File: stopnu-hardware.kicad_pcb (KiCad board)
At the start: 4 copper layers, 150 x 128 mm, 47 parts, among them CN1 SM04B-SRSS-TB (LF)(SN), Q1 TEPT4400, U1 WIFI_KIT_32__V3_, U2 LTV-817M, U26 74LVC1G17GW,125, U3 LTV-817M, U4 LTV-817M

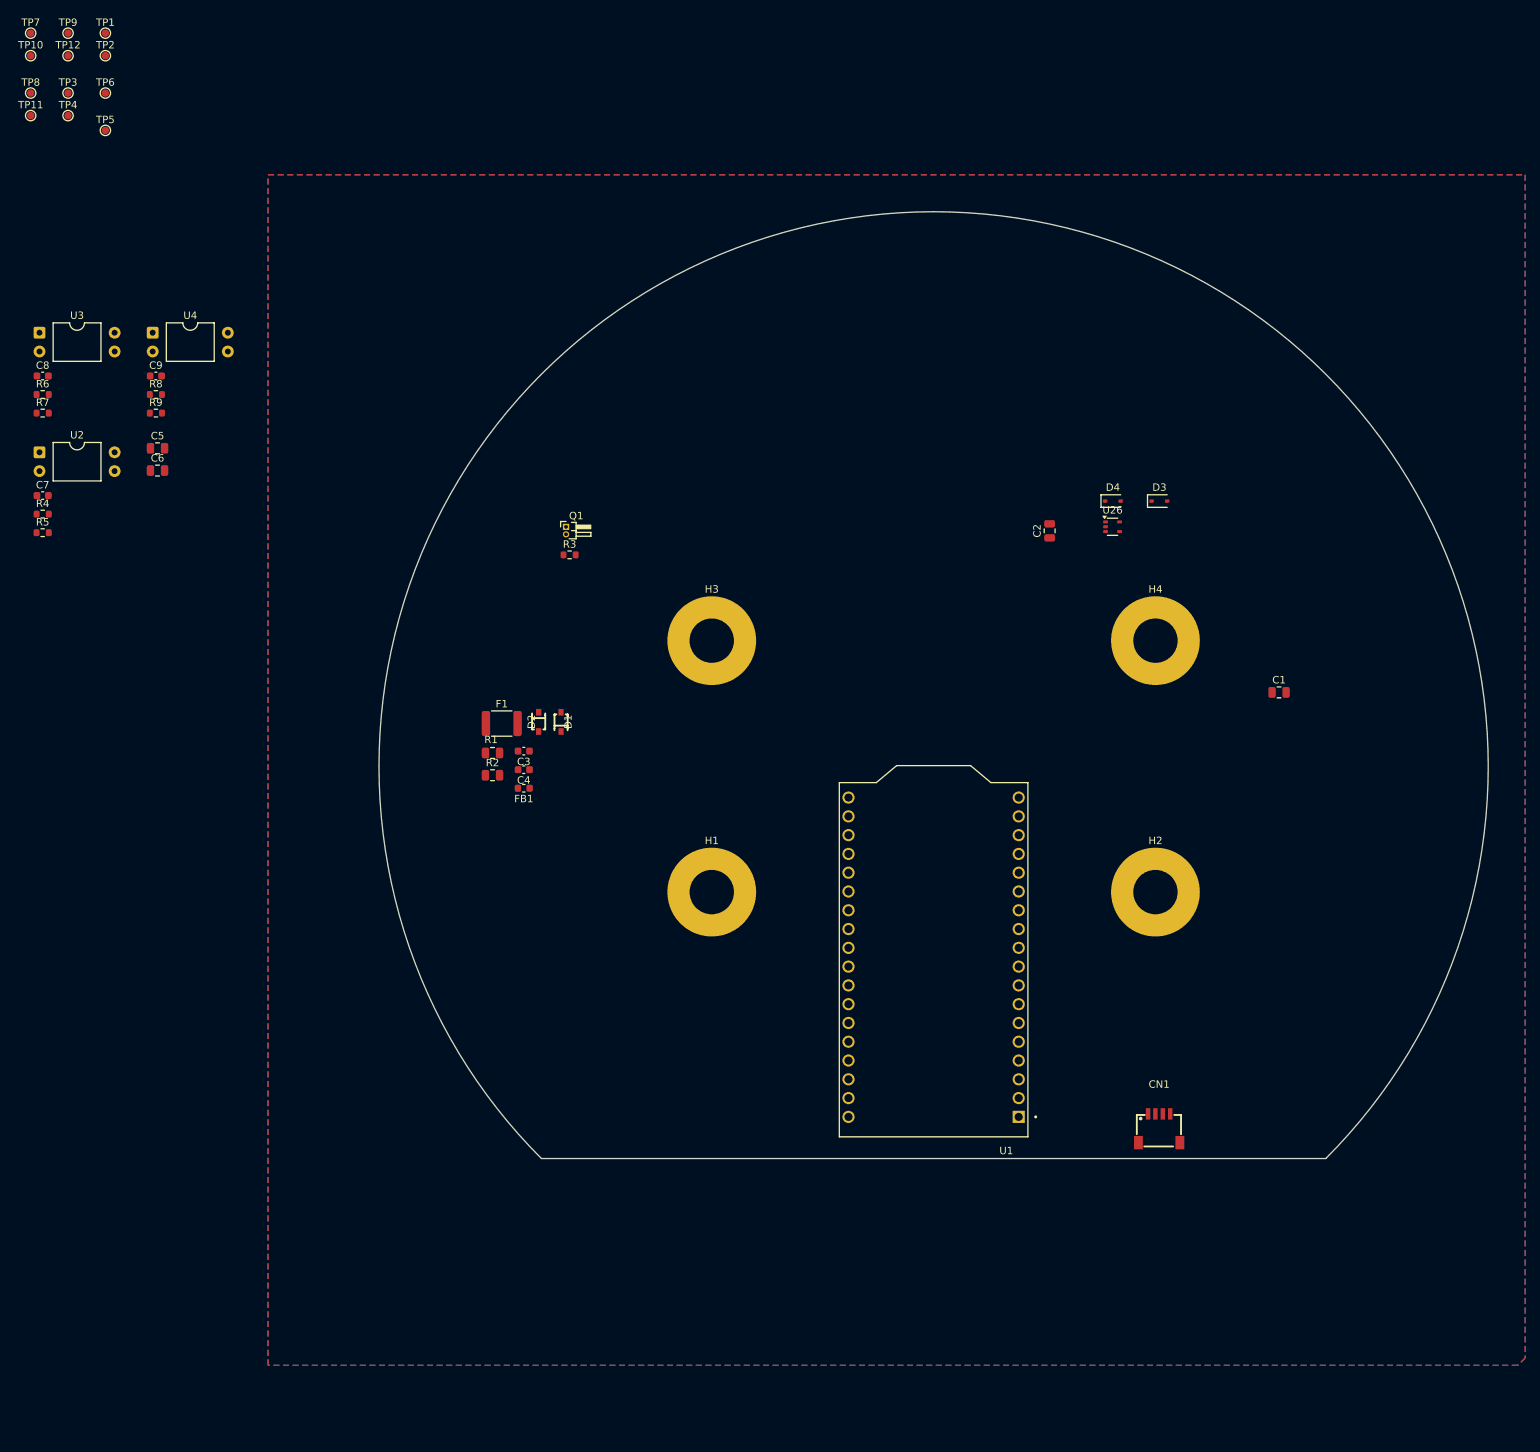
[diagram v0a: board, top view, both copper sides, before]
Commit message: Place opto couplers and some connectors.
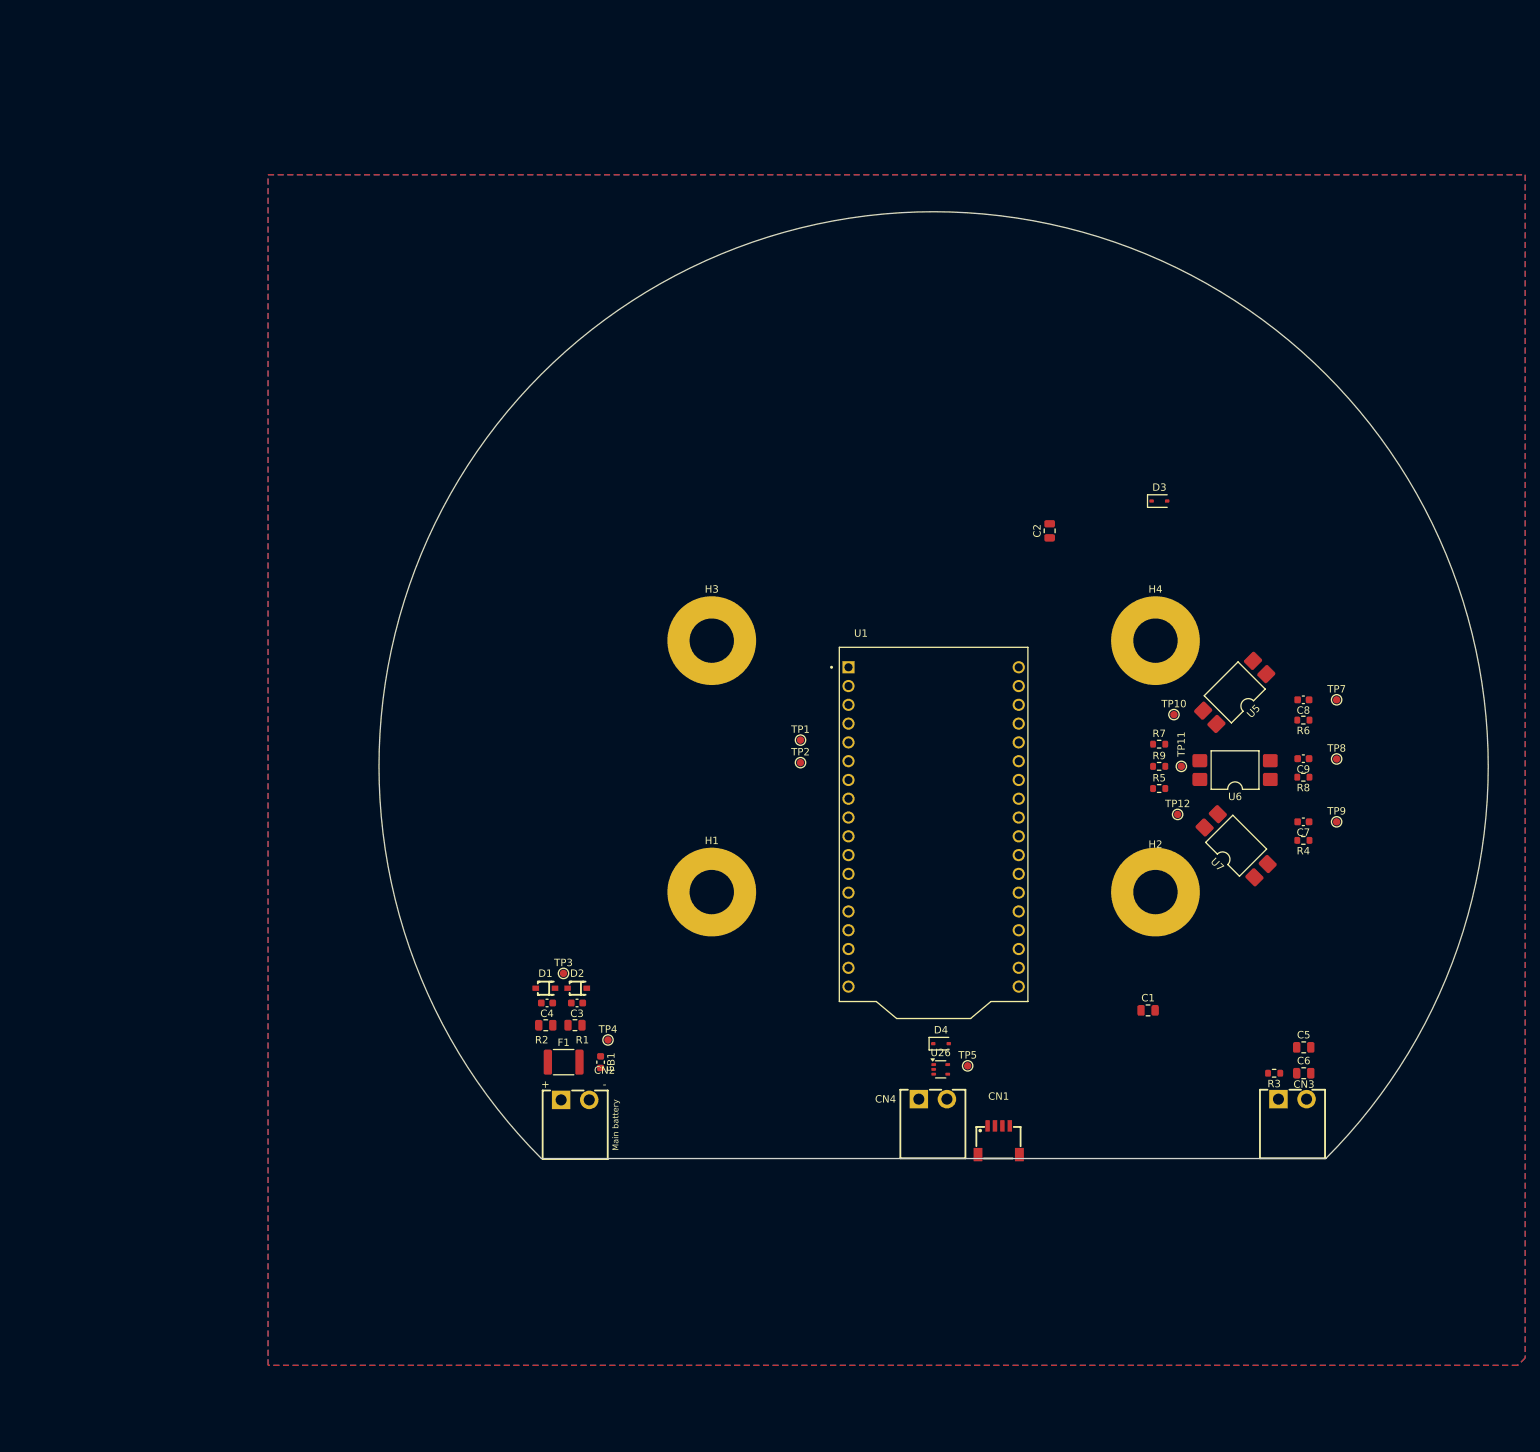
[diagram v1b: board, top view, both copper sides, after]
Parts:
- removed Q1: TEPT4400, Connector_PinHeader_1.00mm:PinHeader_1x02_P1.00mm_Horizontal
- removed TP6: TestPoint, TestPoint:TestPoint_Pad_D1.0mm
- removed U2, U3, U4: LTV-817M, Package_DIP:DIP-4_W10.16mm
- added CN2: OQ0232510000G, lcsc:CONN-TH_OQ0232510000G, F.Cu at (-48.5, 45.1)
- added CN3: OQ0232510000G, lcsc:CONN-TH_OQ0232510000G, F.Cu at (48.5, 45.0)
- added CN4: OQ0232510000G, lcsc:CONN-TH_OQ0232510000G, F.Cu at (-0.10, 45.0)
- added U5: LTV-817S, Package_DIP:SMDIP-4_W9.53mm, F.Cu at (40.7, -10.0)
- added U6: LTV-817S, Package_DIP:SMDIP-4_W9.53mm, F.Cu at (40.8, 0.50)
- added U7: LTV-817S, Package_DIP:SMDIP-4_W9.53mm, F.Cu at (40.9, 10.7)
- moved TP9 202.0 mm to (54.5, 7.50)
- moved TP7 198.3 mm to (54.5, -9.00)
- moved TP8 198.2 mm to (54.5, -1.00)
- moved TP12 181.8 mm to (33.0, 6.50)
- moved TP11 178.8 mm to (33.5, 0.00), turned to 90 degrees
- moved TP10 178.4 mm to (32.5, -7.00)
- moved C7 176.1 mm to (50.0, 7.50), turned to 180 degrees
- moved R4 176.1 mm to (50.0, 10.0), turned to 180 degrees
- moved R6 176.1 mm to (50.0, -6.25), turned to 180 degrees
- moved C8 176.0 mm to (50.0, -9.00), turned to 180 degrees
- moved C6 175.1 mm to (50.0, 41.5)
- moved C5 174.9 mm to (50.0, 38.0)
- moved TP5 172.0 mm to (4.61, 40.5)
- moved C9 163.6 mm to (50.0, -1.04), turned to 180 degrees
- moved R8 163.6 mm to (50.0, 1.47), turned to 180 degrees
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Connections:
- net /Ambient light sensor/V_AMLIGHT renamed /Ambient light sensor/V_AMLIGHT_EM
- net /battery_50v_to_adc/VBATT_OUT_3V3 renamed /battery_50v_to_adc/VBATT_LVL_OUT_LOW
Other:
- board text added: "USB-C cable Clearance"

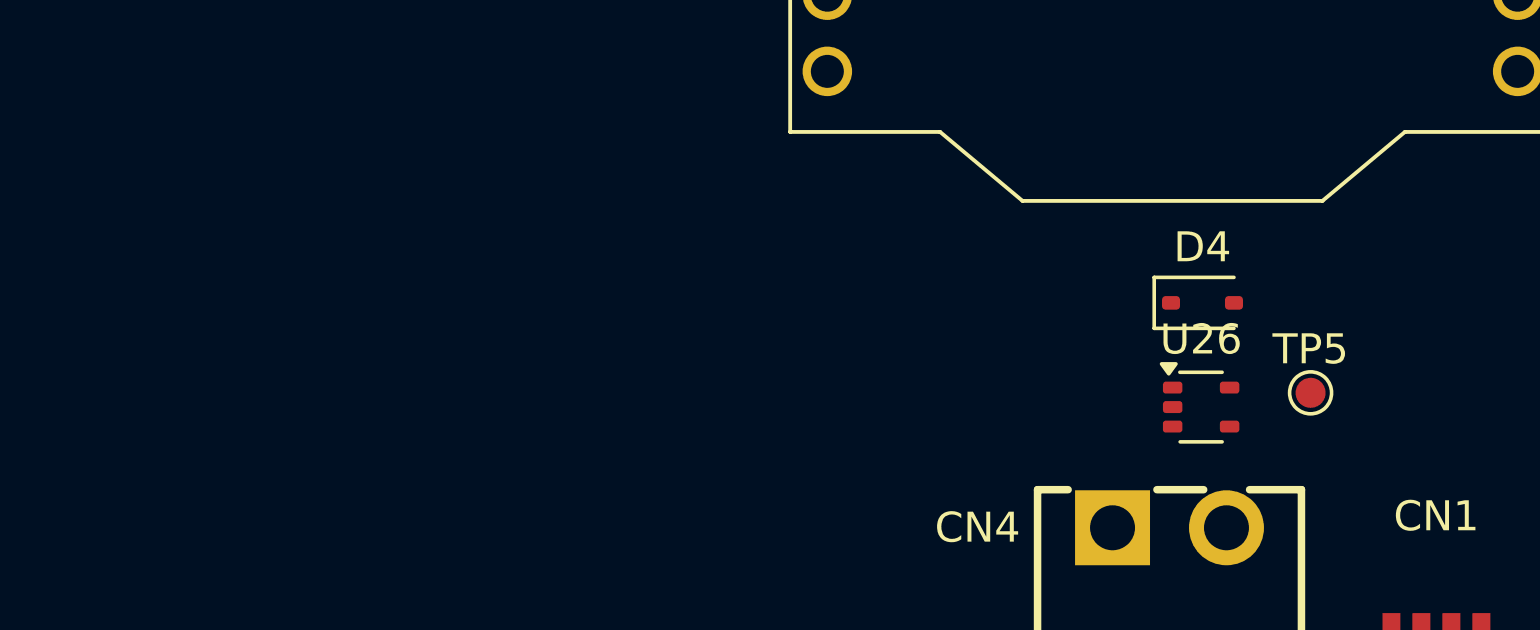
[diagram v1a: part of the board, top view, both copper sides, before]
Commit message: changed driver IC for LED signal to 74HCT1G125GW
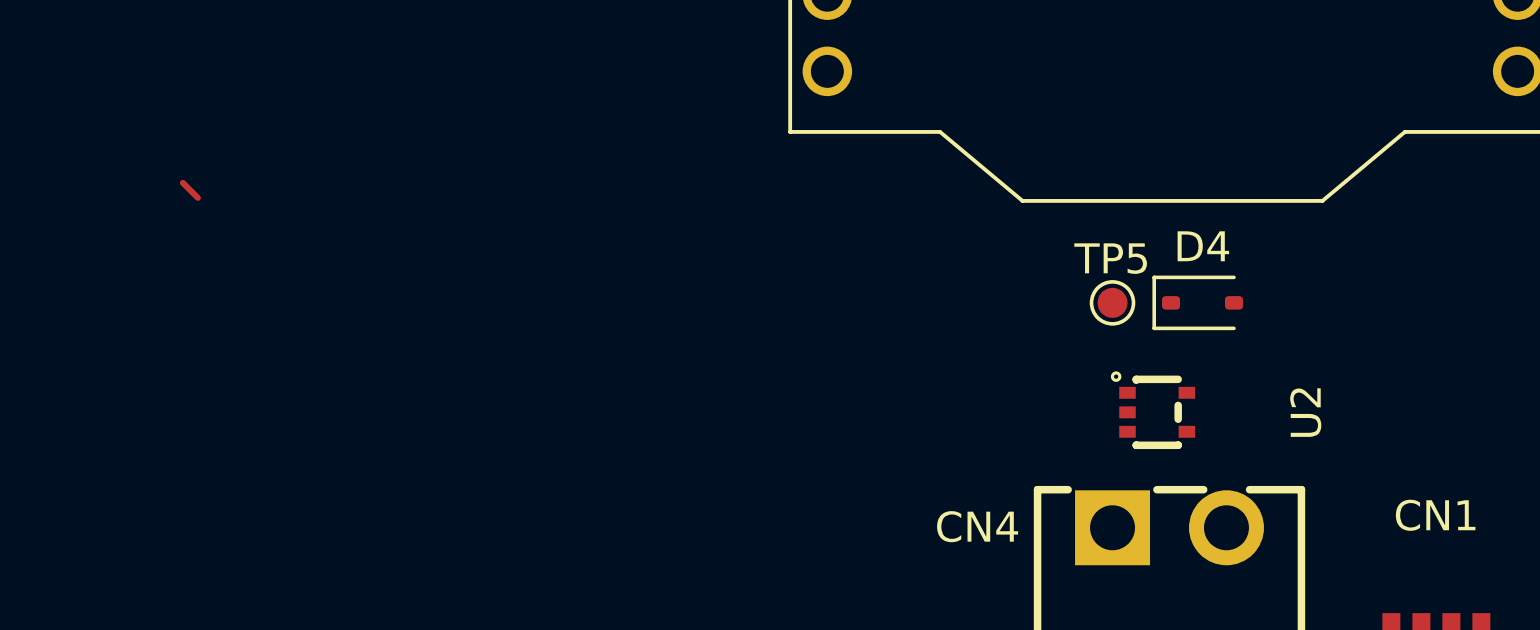
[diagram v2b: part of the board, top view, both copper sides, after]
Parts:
- removed U26: 74LVC1G17GW,125, Package_TO_SOT_SMD:SOT-353_SC-70-5
- added U2: 74HCT1G125GW-Q100H, lcsc:TSSOP-5_L2.1-W1.3-P0.65-LS2.2-BL, F.Cu at (-0.51, 41.1)
- moved TP5 7.25 mm to (-2.00, 37.5)
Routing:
- net (no net): track 0.00 -> 0.71 mm

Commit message: Push schematic stuff missed before.
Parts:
- added C10: 100nF, Capacitor_SMD:C_0805_2012Metric, F.Cu at (19.2, 29.0)
- added C11: C_Small, Capacitor_SMD:C_0603_1608Metric, F.Cu at (25.5, 31.3)
- added C12: C_Small, Capacitor_SMD:C_0603_1608Metric, F.Cu at (64.5, -3.00)
- added C13: C_Small, Capacitor_SMD:C_0603_1608Metric, F.Cu at (64.5, 35.0)
- added C14: C_Small, Capacitor_SMD:C_0603_1608Metric, F.Cu at (8.50, 38.7)
- added C15: 10u, Capacitor_SMD:C_0805_2012Metric, F.Cu at (54.1, -1.09)
- added C16: 100nF, Capacitor_SMD:C_0805_2012Metric, F.Cu at (54.1, 1.92)
- added C62: 10u, Capacitor_SMD:C_0805_2012Metric, F.Cu at (-37.2, 28.8)
- added C63: 10u, Capacitor_SMD:C_0805_2012Metric, F.Cu at (-33.3, 28.8)
- added CN5: OQ0232510000G, lcsc:CONN-TH_OQ0232510000G, F.Cu at (-34.5, 44.6)
- added CN6: OQ0432510000G, lcsc:CONN-TH_4P-P3.81_OQ0432510000G, F.Cu at (57.3, 44.5)
- added FB2: BLM18PG121SN1D, Inductor_SMD:L_0603_1608Metric, F.Cu at (-32.7, 40.1)
- added FB3: BLM18PG121SN1D, Inductor_SMD:L_0603_1608Metric, F.Cu at (-36.2, 40.1)
- added JP1: Jumper_2_Bridged, Jumper:SolderJumper-2_P1.3mm_Bridged_RoundedPad1.0x1.5mm, F.Cu at (17.5, -16.5)
- added JP2: Jumper_2_Open, Jumper:SolderJumper-2_P1.3mm_Open_RoundedPad1.0x1.5mm, F.Cu at (17.4, -20.5)
- added R53: 10k, Resistor_SMD:R_0402_1005Metric, F.Cu at (-30.2, 35.3)
- added R54: 6.8k, Resistor_SMD:R_0402_1005Metric, F.Cu at (-38.2, 35.3)
- added U19: SY6280AAC, Package_TO_SOT_SMD:SOT-23-5, F.Cu at (-34.1, 33.3)
- added U3: LD1117V33, lcsc:TO-220-3_L10.0-W4.5-P2.54-L, F.Cu at (53.5, -6.00)
- FB1: value FerriteBead_Small -> BLM18PG121SN1D
- moved TP10 49.2 mm to (55.5, 36.5)
- moved R7 44.4 mm to (55.5, 33.7), turned to -90 degrees
- moved TP11 44.2 mm to (58.5, 36.5), turned to 180 degrees
- moved R9 43.8 mm to (58.5, 33.7), turned to -90 degrees
- moved R5 37.7 mm to (52.5, 33.7), turned to -90 degrees
- moved C2 37.6 mm to (48.8, -13.9)
- moved U5 35.9 mm to (56.0, 22.5), turned to -90 degrees
- moved TP12 35.8 mm to (52.5, 36.5), turned to 135 degrees
- moved U6 31.4 mm to (63.2, 22.5), turned to -90 degrees
- moved D3 28.8 mm to (18.0, -10.0)
- moved C8 22.6 mm to (54.3, 13.2), turned to -90 degrees
- moved CN1 22.0 mm to (30.8, 49.6)
- moved R6 20.7 mm to (57.1, 13.2), turned to -90 degrees
- moved D4 19.9 mm to (20.9, 37.5)
- moved TP5 19.9 mm to (17.9, 37.5)
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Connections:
- D3 pad 1: +3.3V -> +3V3
- U1 pad J3_2: +3V3 -> /MCU/+3V3MCU
- U1 pad J3_3: +3V3 -> /MCU/+3V3MCU
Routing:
- net /battery_50v_to_adc/VBATT_LVL_OUT_LOW: track 0.00 -> 14.0 mm
- net /battery_50v_to_adc/VBATT_3_V50: track 0.00 -> 6.67 mm
- net /battery_50v_to_adc/VBATT_V50: track 0.00 -> 5.44 mm
- net /battery_50v_to_adc/VBATT_2_V50: track 0.00 -> 3.19 mm
- net VBATT: track 0.00 -> 2.54 mm
- net (no net): track 0.71 -> 0.00 mm
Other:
- board size 150 x 128 mm -> 140 x 106 mm
- board text added: "Bracket housing stay out"

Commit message: Some extra work for building the rats nest.
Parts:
- removed C10: 100nF, Capacitor_SMD:C_0805_2012Metric
- removed C3, C4: 10nF, Capacitor_SMD:C_0603_1608Metric
- removed CN2: OQ0232510000G, lcsc:CONN-TH_OQ0232510000G
- removed D1, D2: 1N4148WSG_C2904852, lcsc:SOD-323_L1.6-W1.3-LS2.7-RD
- removed F1: Polyfuse, Fuse:Fuse_1812_4532Metric
- removed FB1: BLM18PG121SN1D, Inductor_SMD:L_0603_1608Metric
- removed R1: 100k, Capacitor_SMD:C_0805_2012Metric
- removed R2: 3.6K, Capacitor_SMD:C_0805_2012Metric
- removed TP3, TP4: TestPoint, TestPoint:TestPoint_Pad_D1.0mm
- added J1: Conn_02x15_Odd_Even, Connector_PinHeader_2.54mm:PinHeader_2x15_P2.54mm_Horizontal, F.Cu at (-18.8, 14.0)
- H1, H2, H3, H4: footprint MountingHole:MountingHole_6mm_Pad -> MountingHole:MountingHole_6.4mm_M6_DIN965_Pad
- moved U3 81.6 mm to (-27.2, 6.19)
- moved C15 81.0 mm to (-26.0, 10.8), turned to -90 degrees
- moved C16 78.2 mm to (-23.0, 14.7), turned to -90 degrees
- moved D3 76.1 mm to (-20.3, 55.8), turned to 90 degrees
- moved C2 74.7 mm to (5.36, 46.9)
- moved TP8 72.3 mm to (11.8, 62.1), turned to -90 degrees
- moved R8 70.5 mm to (8.89, 57.7), turned to 90 degrees
- moved C9 65.9 mm to (11.9, 57.7), turned to 90 degrees
- moved JP1 64.3 mm to (-41.6, 8.86)
- moved JP2 64.3 mm to (-41.8, 4.86)
- moved C13 63.7 mm to (5.00, 57.7)
- moved TP7 63.6 mm to (19.2, 61.6), turned to -90 degrees
- moved TP1 62.5 mm to (-45.5, 52.6), turned to -90 degrees
- moved TP2 62.0 mm to (-45.5, 55.1), turned to -90 degrees
- moved R6 59.9 mm to (16.4, 57.2), turned to 90 degrees
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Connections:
- net /MCU/GPIO33 renamed /GPIO42
- net /MCU/MCU_VBAT_3V3 renamed /HELTEC V3/MCU_VBAT_3V3
- net Net-(U1A-U0RXD/GPIO44/CP2102_TX) renamed /UART_TX
- net Net-(U1A-U0TXD/GPIO43/CP2102_RX) renamed /UART_RX
- CN1 pad 3: /QWIIC_SDA -> /GPIO47
- CN1 pad 4: /QWIIC_SCL -> /GPIO48
- CN6 pad 2: /Button IO/BUT_OUT_01 -> /Button IO/BUT_IN_03
- CN6 pad 3: /Button IO/BUT_OUT_02 -> /Button IO/BUT_IN_02
- CN6 pad 4: /Button IO/BUT_OUT_03 -> /Button IO/BUT_IN_01
- JP1 pad 2: /MCU/+3V3MCU -> +3V3
- R5 pad 2: /Button IO/BUT_OUT_01 -> /GPIO5
- R7 pad 2: /Button IO/BUT_OUT_02 -> /GPIO6
- R9 pad 2: /Button IO/BUT_OUT_03 -> /GPIO7
- TP10 pad 1: /Button IO/BUT_OUT_02 -> /GPIO6
- TP11 pad 1: /Button IO/BUT_OUT_03 -> /GPIO7
- TP12 pad 1: /Button IO/BUT_OUT_01 -> /GPIO5
- U1 pad J2_10: unconnected-(U1A-GPIO20/U1CTS/ADC2_CH9/CLK_OUT1/USB_D+-PadJ2_10) -> /USB_D+
- U1 pad J2_11: unconnected-(U1A-GPIO19/U1RST/ADC2_CH9/CLK_OUT2/USB_D--PadJ2_11) -> /USB_D-
- U1 pad J2_12: /MCU/GPIO07 -> /GPIO33
- U1 pad J2_13: /MCU/GPIO06 -> /GPIO47
- U1 pad J2_14: /MCU/GPIO05 -> /GPIO48
- U1 pad J2_15: /MCU/GPIO04 -> /GPIO26
- U1 pad J2_7: /MCU/MCU_RST -> /MCU_RST
- U1 pad J2_8: unconnected-(U1A-GPIO0/USER_SW-PadJ2_8) -> /USER_KEY
- U1 pad J2_9: unconnected-(U1A-GPIO21/OLED_RST-PadJ2_9) -> /OLED_RST
- U1 pad J3_10: /MCU/GPIO36 -> /GPIO39
- U1 pad J3_11: /MCU/GPIO37 -> /GPIO38
- U1 pad J3_12: unconnected-(U1B-GPIO38/FSPIWP/SUBSPIWP-PadJ3_12) -> /GPIO01
- U1 pad J3_13: unconnected-(U1B-GPIO39/MTCK-PadJ3_13) -> /GPIO02
- U1 pad J3_14: unconnected-(U1B-GPIO40/MTDO-PadJ3_14) -> /GPIO03
- U1 pad J3_15: unconnected-(U1B-GPIO41/MTDI-PadJ3_15) -> /GPIO04
- U1 pad J3_16: unconnected-(U1B-GPIO42/MTMS-PadJ3_16) -> /GPIO05
- U1 pad J3_17: /MCU/GPIO45 -> /GPIO06
- U1 pad J3_18: /MCU/GPIO46 -> /GPIO07
- U1 pad J3_2: /MCU/+3V3MCU -> +3V3
- U1 pad J3_3: /MCU/+3V3MCU -> +3V3
- U1 pad J3_5: /MCU/GPIO48 -> unconnected-(U1B-GPIO46-PadJ3_5)
- U1 pad J3_6: /MCU/GPIO47 -> unconnected-(U1B-GPIO45-PadJ3_6)
- U1 pad J3_8: /MCU/GPIO34 -> /GPIO41
- U1 pad J3_9: /MCU/GPIO35 -> /GPIO40
- U5 pad 4: /Button IO/BUT_OUT_02 -> /GPIO6
- U6 pad 4: /Button IO/BUT_OUT_03 -> /GPIO7
- U7 pad 4: /Button IO/BUT_OUT_01 -> /GPIO5
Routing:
- net /battery_50v_to_adc/VBATT_LVL_OUT_LOW: track 14.0 -> 0.00 mm
- net /battery_50v_to_adc/VBATT_3_V50: track 6.67 -> 0.00 mm
- net /battery_50v_to_adc/VBATT_V50: track 5.44 -> 0.00 mm
- net /battery_50v_to_adc/VBATT_2_V50: track 3.19 -> 0.00 mm
- net VBATT: track 2.54 -> 0.00 mm
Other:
- board size 140 x 106 mm -> 94 x 131 mm
- board text removed: "USB-C cable Clearance"
